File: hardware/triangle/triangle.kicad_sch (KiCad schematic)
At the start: 55 parts, among them J1 Conn_01x02_Socket, J2 Conn_01x02_Socket

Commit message: routing efforts for the triangle
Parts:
- J1, J2: footprint Connector_JST:JST_PH_S2B-PH-SM4-TB_1x02-1MP_P2.00mm_Horizontal -> footprints:CONN-SMD_ZX-XH2.54-2PLT; JLCPCB Part # (none) -> C7429680
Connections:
- net 5V POWER is gone; now on net 5V Power: D1.4 (VDD), D10.4 (VDD), D11.4 (VDD), D12.4 (VDD), D13.4 (VDD), D14.4 (VDD), D15.4 (VDD), D16.4 (VDD), D17.4 (VDD), D18.4 (VDD), D19.4 (VDD), D2.4 (VDD), D20.4 (VDD), D21.4 (VDD), D22.4 (VDD), D23.4 (VDD), D24.4 (VDD), D3.4 (VDD), D4.4 (VDD), D5.4 (VDD), D6.4 (VDD), D7.4 (VDD), D8.4 (VDD), D9.4 (VDD)
- net 5V Power: now also J2.1 (Pin_1)
- net GND: now also J2.2 (Pin_2)
- net LED_DATA_IN: now also J1.1 (Pin_1)
- net LED_DATA_OUT: now also J1.2 (Pin_2)
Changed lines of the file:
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@@
 		)
 	)
-	(global_label "5V POWER"
+	(global_label "5V Power"
+		(shape output)
+		(at 93.98 173.355 180)
+		(fields_autoplaced yes)
+		(effects
+			(font
+				(size 1.27 1.27)
+			)
+			(justify right)
+		)
+		(property "Intersheetrefs" "${INTERSHEET_REFS}"
+			(at 82.1048 173.355 0)
+			(hide yes)
+			(show_name no)
+			(do_not_autoplace no)
+			(effects
+				(font
+					(size 1.27 1.27)
+				)
+				(justify right)
+			)
+		)
+	)
+	(global_label "5V Power"
 		(shape input)
 		(at 150.495 19.05 0)
@@
 		)
 		(property "Intersheetrefs" "${INTERSHEET_REFS}"
-			(at 163.2168 19.05 0)
+			(at 162.3702 19.05 0)
 			(hide yes)
 			(show_name no)
@@
 		)
 	)
+	(global_label "LED_DATA_OUT"
+		(shape input)
+		(at 93.98 168.275 180)
+		(fields_autoplaced yes)
+		(effects
+			(font
+				(size 1.27 1.27)
+			)
+			(justify right)
+		)
+		(property "Intersheetrefs" "${INTERSHEET_REFS}"
+			(at 77.5691 168.275 0)
+			(hide yes)
+			(show_name no)
+			(do_not_autoplace no)
+			(effects
+				(font
+					(size 1.27 1.27)
+				)
+				(justify right)
+			)
+		)
+	)
+	(global_label "LED_DATA_IN"
+		(shape output)
+		(at 93.98 165.735 180)
+		(fields_autoplaced yes)
+		(effects
+			(font
+				(size 1.27 1.27)
+			)
+			(justify right)
+		)
+		(property "Intersheetrefs" "${INTERSHEET_REFS}"
+			(at 79.2624 165.735 0)
+			(hide yes)
+			(show_name no)
+			(do_not_autoplace no)
+			(effects
+				(font
+					(size 1.27 1.27)
+				)
+				(justify right)
+			)
+		)
+	)
 	(global_label "LED_DATA_IN"
 		(shape input)
@@
 			)
 		)
-		(property "Footprint" "Connector_JST:JST_PH_S2B-PH-SM4-TB_1x02-1MP_P2.00mm_Horizontal"
+		(property "Footprint" "footprints:CONN-SMD_ZX-XH2.54-2PLT"
 			(at 99.06 173.355 0)
 			(hide yes)
@@
 			)
 		)
+		(property "JLCPCB Part #" "C7429680"
+			(at 99.06 173.355 0)
+			(hide yes)
+			(show_name no)
+			(do_not_autoplace no)
+			(effects
+				(font
+					(size 1.27 1.27)
+				)
+			)
+		)
 		(pin "2"
 		)
@@
 			)
 		)
-		(property "Footprint" "Connector_JST:JST_PH_S2B-PH-SM4-TB_1x02-1MP_P2.00mm_Horizontal"
+		(property "Footprint" "footprints:CONN-SMD_ZX-XH2.54-2PLT"
 			(at 99.06 165.735 0)
 			(hide yes)
@@
 			)
 		)
+		(property "JLCPCB Part #" "C7429680"
+			(at 99.06 165.735 0)
+			(hide yes)
+			(show_name no)
+			(do_not_autoplace no)
+			(effects
+				(font
+					(size 1.27 1.27)
+				)
+			)
+		)
 		(pin "2"
 		)
@@
 					(unit 1)
 				)
+			)
+		)
+	)
+	(symbol
+		(lib_id "power:GND")
+		(at 93.98 175.895 270)
+		(unit 1)
+		(body_style 1)
+		(exclude_from_sim no)
+		(in_bom yes)
+		(on_board yes)
+		(in_pos_files yes)
+		(dnp no)
+		(fields_autoplaced yes)
+		(property "Reference" "#PWR01"
+			(at 87.63 175.895 0)
+			(hide yes)
+			(show_name no)
+			(do_not_autoplace no)
+			(effects
+				(font
+					(size 1.27 1.27)
+				)
+			)
+		)
+		(property "Value" "GND"
+			(at 90.17 175.8949 90)
+			(show_name no)
+			(do_not_autoplace no)
+			(effects
+				(font
+					(size 1.27 1.27)
+				)
+				(justify right)
+			)
+		)
+		(property "Footprint" ""
+			(at 93.98 175.895 0)
+			(hide yes)
+			(show_name no)
+			(do_not_autoplace no)
+			(effects
+				(font
+					(size 1.27 1.27)
+				)
+			)
+		)
+		(property "Datasheet" ""
+			(at 93.98 175.895 0)
+			(hide yes)
+			(show_name no)
+			(do_not_autoplace no)
+			(effects
+				(font
+					(size 1.27 1.27)
+				)
+			)
+		)
+		(property "Description" "Power symbol creates a global label with name \"GND\" , ground"
+			(at 93.98 175.895 0)
+			(hide yes)
+			(show_name no)
+			(do_not_autoplace no)
+			(effects
+				(font
+					(size 1.27 1.27)
+				)
+			)
+		)
+		(pin "1"
+		)
+		(instances
+			(project "triangle"
+				(path "/f9839f04-8b32-4f6f-9cb5-92c3ed04dc78"
+					(reference "#PWR01")
+					(unit 1)
+				)

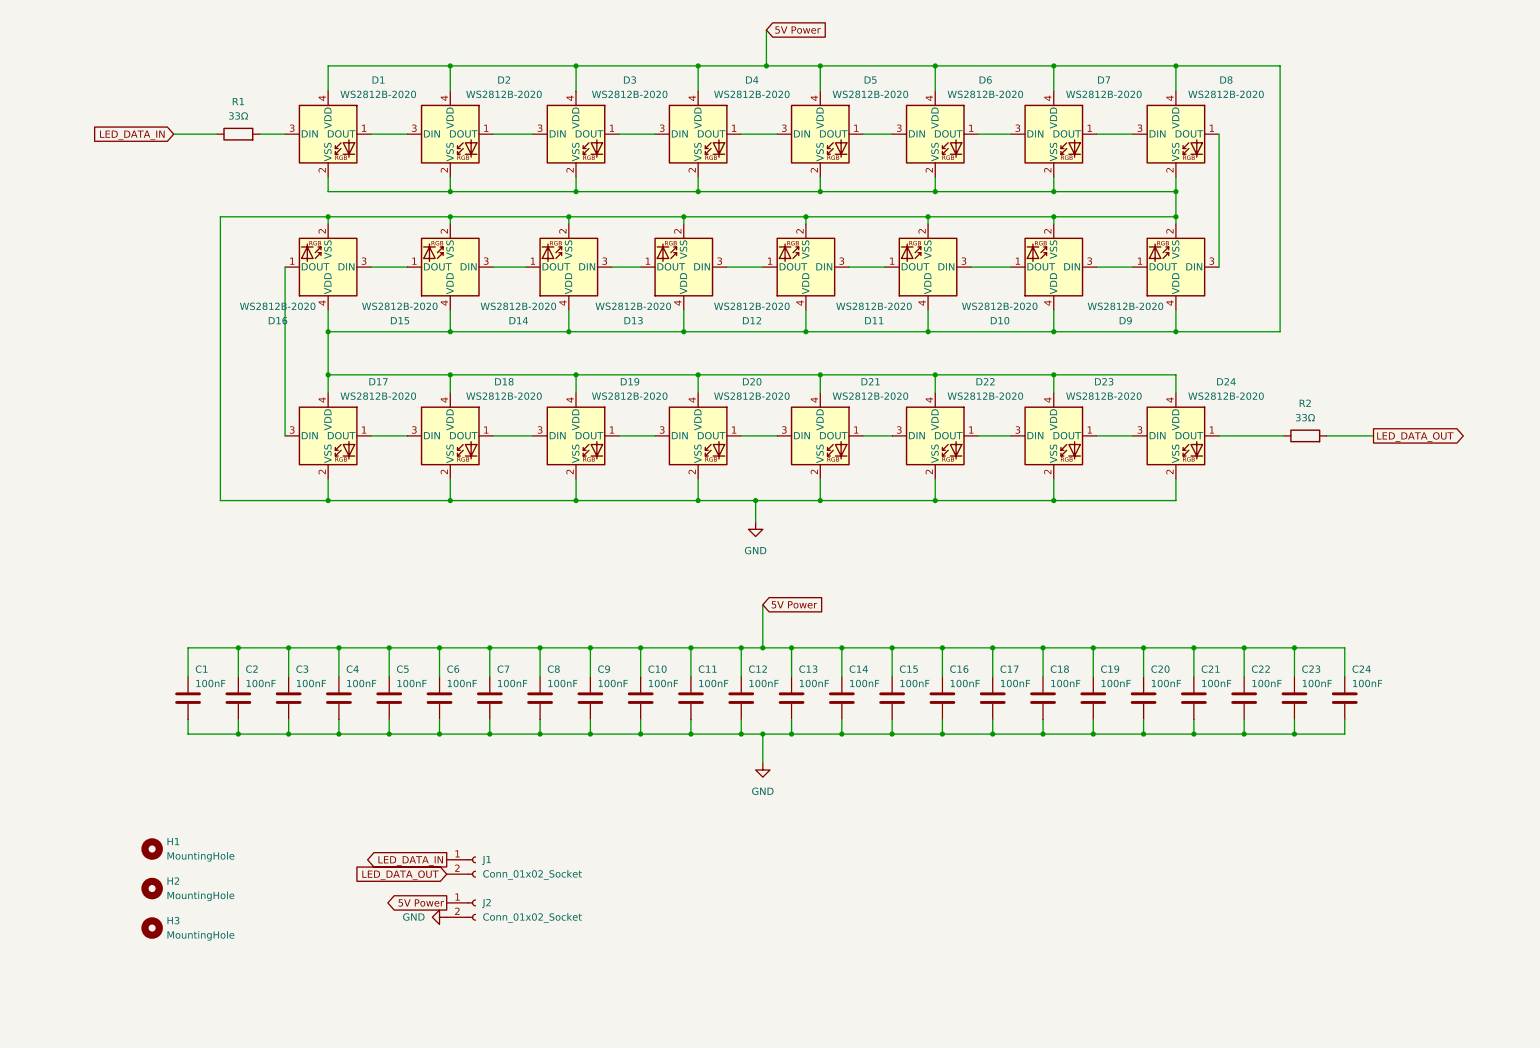
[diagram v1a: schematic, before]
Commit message: fix routing and add test points
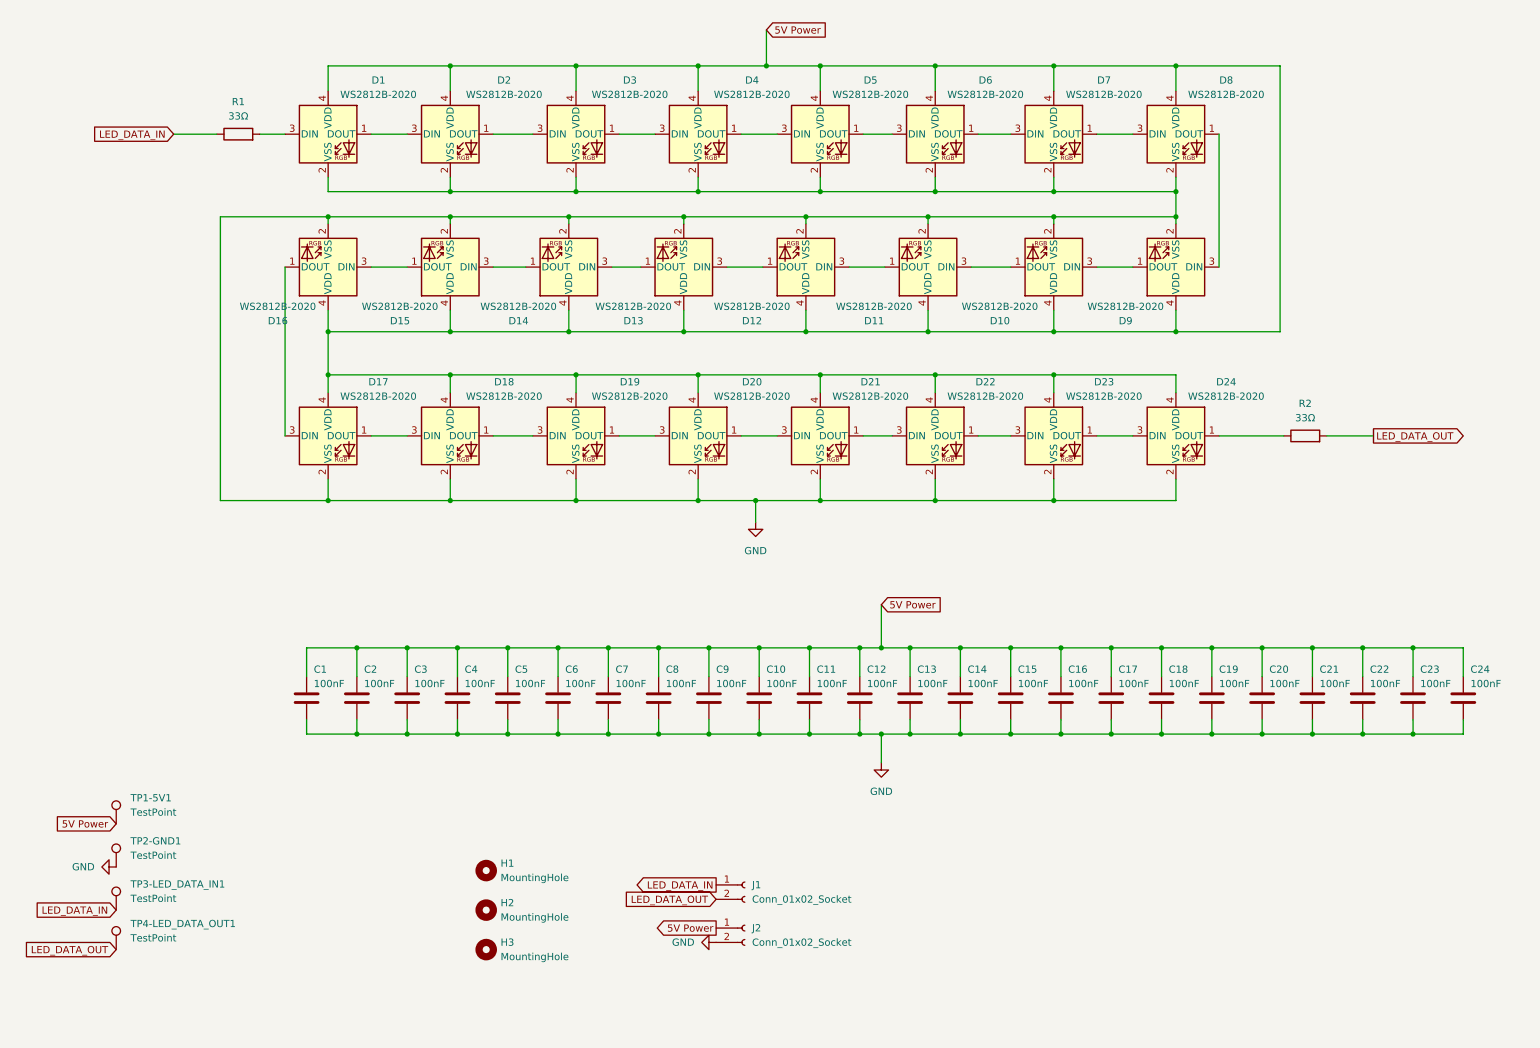
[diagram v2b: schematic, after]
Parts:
- added TP1-5V1, TP2-GND1, TP3-LED_DATA_IN1, TP4-LED_DATA_OUT1: TestPoint, TestPoint:TestPoint_Pad_1.0x1.0mm, symbol Connector:TestPoint
- D1, D10, D11, D12, D13, D14, D15, D16, D17, D18, D19, D2, D20, D21, D22, D23, D24, D3, D4, D5, D6, D7, D8, D9: footprint LED_SMD:LED_WS2812B-2020_PLCC4_2.0x2.0mm -> footprints:LED_WS2812B-2020_PLCC4_2.0x2.0mm - no silkscreen
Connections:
- net 5V Power: now also TP1-5V1.1
- net GND: now also TP2-GND1.1
- net LED_DATA_IN: now also TP3-LED_DATA_IN1.1
- net LED_DATA_OUT: now also TP4-LED_DATA_OUT1.1
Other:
- moved on the sheet: C1, C10, C11, C12, C13, C14, C15, C16, C17, C18, C19, C2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

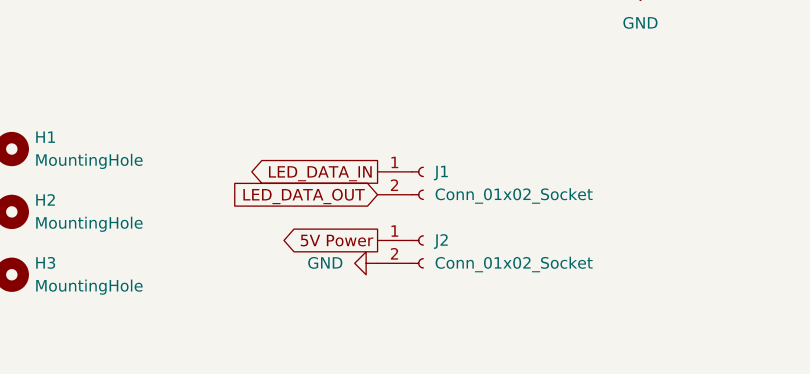
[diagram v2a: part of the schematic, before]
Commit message: add cap to triangle board and start controller board
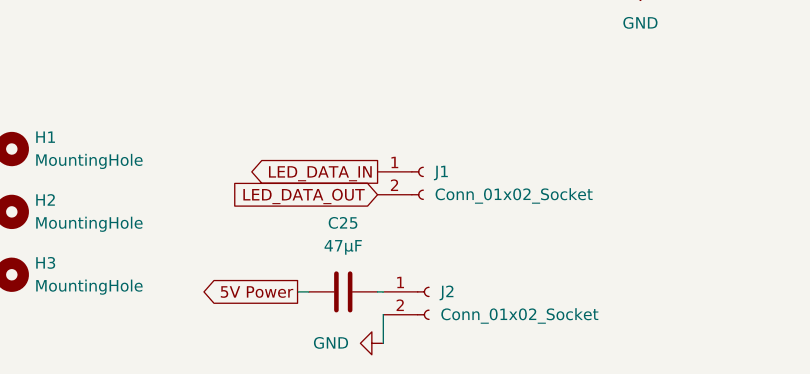
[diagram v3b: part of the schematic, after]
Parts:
- added C25: 47µF, Capacitor_SMD:C_1206_3216Metric, symbol Device:C
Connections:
- net 5V Power: now also C25.1; no longer J2.1 (Pin_1)
- new net: C25.2, J2.1 (Pin_1)
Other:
- moved on the sheet: J2
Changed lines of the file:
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@@
 	(wire
 		(pts
+			(xy 132.715 183.515) (xy 133.985 183.515)
+		)
+		(stroke
+			(width 0)
+			(type default)
+		)
+	)
+	(wire
+		(pts
 			(xy 115.57 52.07) (xy 115.57 53.34)
 		)
@@
 	(wire
 		(pts
+			(xy 142.24 189.23) (xy 142.24 186.055)
+		)
+		(stroke
+			(width 0)
+			(type default)
+		)
+	)
+	(wire
+		(pts
 			(xy 157.48 52.07) (xy 179.07 52.07)
 		)
@@
 	(wire
 		(pts
+			(xy 141.605 183.515) (xy 142.24 183.515)
+		)
+		(stroke
+			(width 0)
+			(type default)
+		)
+	)
+	(wire
+		(pts
 			(xy 104.775 143.51) (xy 113.665 143.51)
 		)
@@
 	(global_label "5V Power"
 		(shape output)
-		(at 141.605 177.8 180)
+		(at 132.715 183.515 180)
 		(fields_autoplaced yes)
 		(effects
@@
 		)
 		(property "Intersheetrefs" "${INTERSHEET_REFS}"
-			(at 129.7298 177.8 0)
+			(at 120.8398 183.515 0)
 			(hide yes)
 			(show_name no)
@@
 	)
 	(symbol
+		(lib_id "Device:C")
+		(at 137.795 183.515 90)
+		(unit 1)
+		(body_style 1)
+		(exclude_from_sim no)
+		(in_bom yes)
+		(on_board yes)
+		(in_pos_files yes)
+		(dnp no)
+		(fields_autoplaced yes)
+		(property "Reference" "C25"
+			(at 137.795 175.895 90)
+			(show_name no)
+			(do_not_autoplace no)
+			(effects
+				(font
+					(size 1.27 1.27)
+				)
+			)
+		)
+		(property "Value" "47µF"
+			(at 137.795 178.435 90)
+			(show_name no)
+			(do_not_autoplace no)
+			(effects
+				(font
+					(size 1.27 1.27)
+				)
+			)
+		)
+		(property "Footprint" "Capacitor_SMD:C_1206_3216Metric"
+			(at 141.605 182.5498 0)
+			(hide yes)
+			(show_name no)
+			(do_not_autoplace no)
+			(effects
+				(font
+					(size 1.27 1.27)
+				)
+			)
+		)
+		(property "Datasheet" "https://jlc-prod-smt.oss-eu-central-1.aliyuncs.com/smtDataManualFile/8586178840691683328-C77101.pdf?response-content-disposition=attachment%3B%20filename%3DC77101.pdf%3B%20filename%2A%3DUTF-8%27%27C77101.pdf&x-oss-date=20260530T174020Z&x-oss-expires=1800&x-oss-security-token=CAISgAN1q6Ft5B2yfSjIr5n%2Bfdvem%2Bts05SjcVeCpXNkYt5rmo3Mrzz2IHhMdHJsAOodtv0%2FmmhT6PkclqRLcbhpcmfjV%2BZHzLB8qbk31zBO4J7b16cNrbH4M4H6aXeirtuwDsz9SNTCALjPD3nPii50x5bjaDymRCbLGJaViJlhHLN1Ow6jdmhpCctxLAlvo9NgFxm3D%2Fu2NQPwiWf9FVdhvhEG6Vly8qOi2MaRmFy8yFTx0b0SvJ%2BjYMrmPctoN9JnSdC5mfdzau3a1TJ84gRD0a5wkaVA1zbDs5bfISEIuUzebreLqY03dV4mOvdqIcMe8qigz88fk%2FfIioH6xyxKOexoSCnFTOiiupCcQLPyao9jLu6iayqViY7QaIOTqQohZmkAMwVOasAsI3Ngh4zF97Qt0cVNkXO9gWfLI8DtuMleWkppw9R5cnSgc5lCkRRYwGs1287ugXlSQzo890KPDAEovaKCnZ2ZSfh7Y4sNknI6i%2Bfc2Se2MIkIWjBNb6KWD5sagAGr5rmBvHeFC8TZ%2BJcd86gyYT9ErQ9X%2B0arh9aBqEUpMV00uZssw%2BpJ0wDNLR3IfY4Emrombd1Qhrr0MuB3K8fJjJk9FM3xSkdaC6wlZzPtmjTVgp5eXx0QJhMfflRGyQBUK%2FfqX4UcQ0%2FVp31Qo2ufdtTd4b5xoRPi6Re0vJceYCAA&x-oss-signature-version=OSS4-HMAC-SHA256&x-oss-credential=STS.NZK6ajv4MdVHsq3As1nQGuHgM%2F20260530%2Feu-central-1%2Foss%2Faliyun_v4_request&x-oss-signature=60c0d3c6bb64dcbae917457d6a6bcf0bef18835ea05f75f079bc953471331657"
+			(at 137.795 183.515 0)
+			(hide yes)
+			(show_name no)
+			(do_not_autoplace no)
+			(effects
+				(font
+					(size 1.27 1.27)
+				)
+			)
+		)
+		(property "Description" "Unpolarized capacitor"
+			(at 137.795 183.515 0)
+			(hide yes)
+			(show_name no)
+			(do_not_autoplace no)
+			(effects
+				(font
+					(size 1.27 1.27)
+				)
+			)
+		)
+		(property "JLCPCB Part #" "C77101"
+			(at 137.795 183.515 0)
+			(hide yes)
+			(show_name no)
+			(do_not_autoplace no)
+			(effects
+				(font
+					(size 1.27 1.27)
+				)
+			)
+		)
+		(pin "1"
+		)
+		(pin "2"
+		)
+		(instances
+			(project "triangle"
+				(path "/f9839f04-8b32-4f6f-9cb5-92c3ed04dc78"
+					(reference "C25")
+					(unit 1)
+				)
+			)
+		)
+	)
+	(symbol
 		(lib_id "LED:WS2812B-2020")
 		(at 160.02 37.465 0)
@@
 	(symbol
 		(lib_id "Connector:Conn_01x02_Socket")
-		(at 146.685 177.8 0)
+		(at 147.32 183.515 0)
 		(unit 1)
 		(body_style 1)
@@
 		(fields_autoplaced yes)
 		(property "Reference" "J2"
-			(at 147.955 177.7999 0)
+			(at 148.59 183.5149 0)
 			(show_name no)
 			(do_not_autoplace no)
@@
 		)
 		(property "Value" "Conn_01x02_Socket"
-			(at 147.955 180.3399 0)
+			(at 148.59 186.0549 0)
 			(show_name no)
 			(do_not_autoplace no)
@@
 		)
 		(property "Footprint" "footprints:CONN-SMD_ZX-XH2.54-2PLT"
-			(at 146.685 177.8 0)
+			(at 147.32 183.515 0)
 			(hide yes)
 			(show_name no)
@@
 		)
 		(property "Datasheet" ""
-			(at 146.685 177.8 0)
+			(at 147.32 183.515 0)
 			(hide yes)
 			(show_name no)
@@
 		)
 		(property "Description" "Generic connector, single row, 01x02, script generated"
-			(at 146.685 177.8 0)
+			(at 147.32 183.515 0)
 			(hide yes)
 			(show_name no)
@@
 		)
 		(property "JLCPCB Part #" "C7429680"
-			(at 146.685 177.8 0)
+			(at 147.32 183.515 0)
 			(hide yes)
 			(show_name no)
@@
 	(symbol
 		(lib_id "power:GND")
-		(at 141.605 180.34 270)
+		(at 142.24 189.23 270)
 		(unit 1)
 		(body_style 1)
@@
 		(fields_autoplaced yes)
 		(property "Reference" "#PWR01"
-			(at 135.255 180.34 0)
+			(at 135.89 189.23 0)
 			(hide yes)
 			(show_name no)
@@
 		)
 		(property "Value" "GND"
-			(at 137.795 180.3399 90)
+			(at 138.43 189.2299 90)
 			(show_name no)
 			(do_not_autoplace no)
@@
 		)
 		(property "Footprint" ""
-			(at 141.605 180.34 0)
+			(at 142.24 189.23 0)
 			(hide yes)
 			(show_name no)
@@
 		)
 		(property "Datasheet" ""
-			(at 141.605 180.34 0)
+			(at 142.24 189.23 0)
 			(hide yes)
 			(show_name no)
@@
 		)
 		(property "Description" "Power symbol creates a global label with name \"GND\" , ground"
-			(at 141.605 180.34 0)
+			(at 142.24 189.23 0)
 			(hide yes)
 			(show_name no)

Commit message: use different socket for data vs power to avoid accidents
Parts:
- J1: footprint footprints:CONN-SMD_ZX-XH2.54-2PLT -> footprints:CONN-SMD_B2B-PH-SM4-TBT-LF-SN; JLCPCB Part # C7429680 -> C265003
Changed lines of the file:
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@@
 			)
 		)
-		(property "Footprint" "footprints:CONN-SMD_ZX-XH2.54-2PLT"
+		(property "Footprint" "footprints:CONN-SMD_B2B-PH-SM4-TBT-LF-SN"
 			(at 146.685 170.18 0)
 			(hide yes)
@@
 			)
 		)
-		(property "Datasheet" ""
+		(property "Datasheet" "https://jlc-prod-smt.oss-eu-central-1.aliyuncs.com/smtDataManualFile/8588902703158607872-C265003.pdf?response-content-disposition=attachment%3B%20filename%3DC265003.pdf%3B%20filename%2A%3DUTF-8%27%27C265003.pdf&x-oss-date=20260530T184618Z&x-oss-expires=1800&x-oss-security-token=CAISgAN1q6Ft5B2yfSjIr5mMGOPH2b5C56u6RmrwoVgfesNa3pGdrjz2IHhMdHJsAOodtv0%2FmmhT6PkclqRLcbhpcmfjV%2BZHzLB8qYMJrTZO4J7b16cNrbH4M4H6aXeirtuwDsz9SNTCALjPD3nPii50x5bjaDymRCbLGJaViJlhHLN1Ow6jdmhpCctxLAlvo9NgFxm3D%2Fu2NQPwiWf9FVdhvhEG6Vly8qOi2MaRmFy8yFTx0b0SvJ%2BjYMrmPctoN9JnSdC5mfdzau3a1TJ84gRD0a5wkaVA1zbDs5bfISEIuUzebreLqY03dV4mOvdqIcMe8qigz88fk%2FfIioH6xyxKOexoSCnFTOiiupCcQLPyao9jLu6iayqViY7QaIOTqQohZmkAMwVOasAsI3Ngh4zF97Qt0cVNkXO9gWfLI8DtuMleWorMUcNC5tHD0eS19jklBdzSlusJRAJJUVBflCeKEaRNSAd3WGhEfM2%2BBt4QT30w5N2u00S8OSMIj6WwtaKWD5sagAEiB9a8Fe3Xz48X2tP6dxg54Vro9nibq7GRPtzBohN8u1QdmxofnrAafgnnqWIAyQYzEZD7Qmyn521BE9LOYbykf0HEMcjUKnha5PhgCA%2BaTkV%2BbWuE1SITzT9cI0CaBUqZ3vKId6FEL2fcnTSF0BDC6iF%2Bhf1ATGD2uciyP2xLKSAA&x-oss-signature-version=OSS4-HMAC-SHA256&x-oss-credential=STS.NZ9SYs4acPiQDLAEXJvLv1T6L%2F20260530%2Feu-central-1%2Foss%2Faliyun_v4_request&x-oss-signature=9be76bdf4ed042f2478c7de920dfc88ba2fe608f5eef2b87c8aebd4d72e4c4dc"
 			(at 146.685 170.18 0)
 			(hide yes)
@@
 			)
 		)
-		(property "JLCPCB Part #" "C7429680"
+		(property "JLCPCB Part #" "C265003"
 			(at 146.685 170.18 0)
 			(hide yes)
